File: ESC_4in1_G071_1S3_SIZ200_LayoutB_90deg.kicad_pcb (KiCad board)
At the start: 4 copper layers, 26 x 27 mm, 150 parts, among them J1 Conn_01x08, U1 STM32G071GBU6, U10 NCP81161MNTBG, U11 SIZ200DT-T1-GE3, U12 NCP81161MNTBG, U13 SIZ200DT-T1-GE3, U14 TPS630701, U15 TPS72733DSE, U16 INA185, U17 STM32G071GBU6, U18 NCP81161MNTBG, U19 SIZ200DT-T1-GE3, U2 NCP81161MNTBG, U20 NCP81161MNTBG, U21 STM32G071GBU6, U22 SIZ200DT-T1-GE3, U23 NCP81161MNTBG, U24 SIZ200DT-T1-GE3, U25 NCP81161MNTBG, U26 SIZ200DT-T1-GE3, U27 NCP81161MNTBG, U28 STM32G071GBU6, U29 SIZ200DT-T1-GE3, U3 SIZ200DT-T1-GE3, U30 NCP81161MNTBG, U31 SIZ200DT-T1-GE3, U4 NCP81161MNTBG, U5 SIZ200DT-T1-GE3, U6 NCP81161MNTBG, U7 SIZ200DT-T1-GE3, U8 NCP81161MNTBG, U9 SIZ200DT-T1-GE3

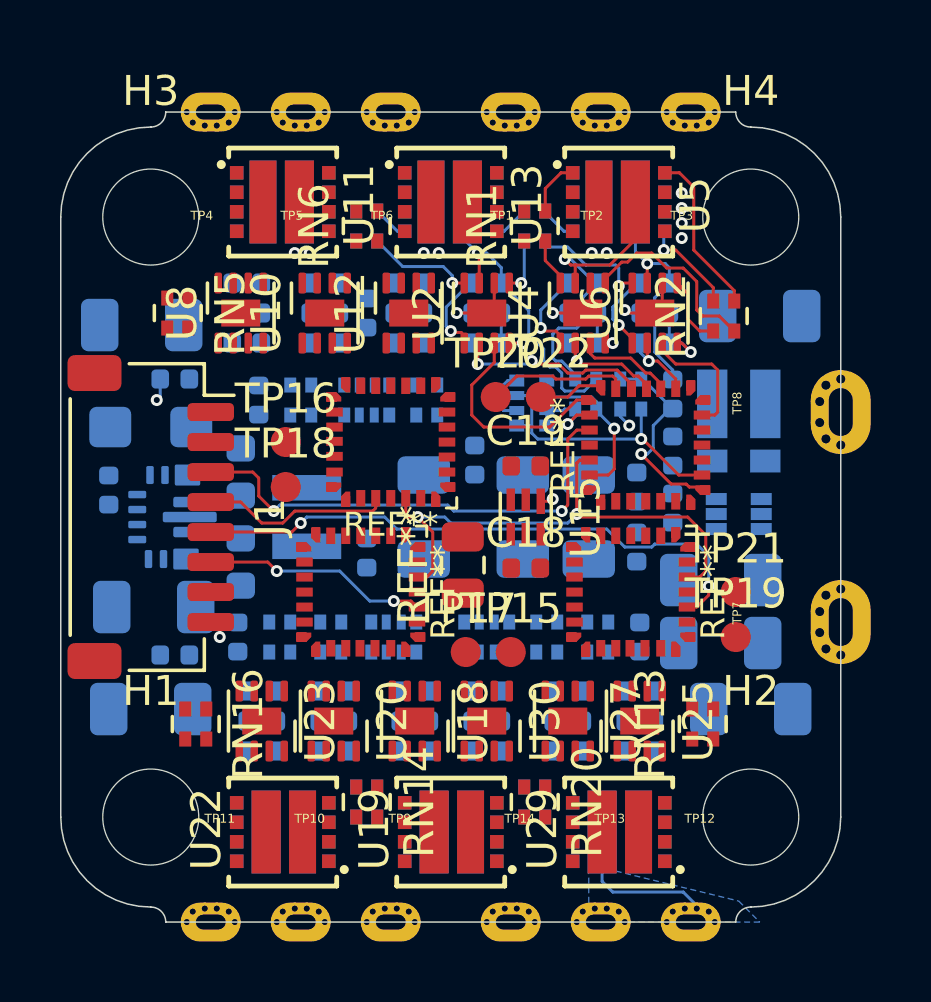
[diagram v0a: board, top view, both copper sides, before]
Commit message: - ESC1 pinout updated - ESC1 schematic done - ESC1 routed - increased PCB size to 26*27 mm
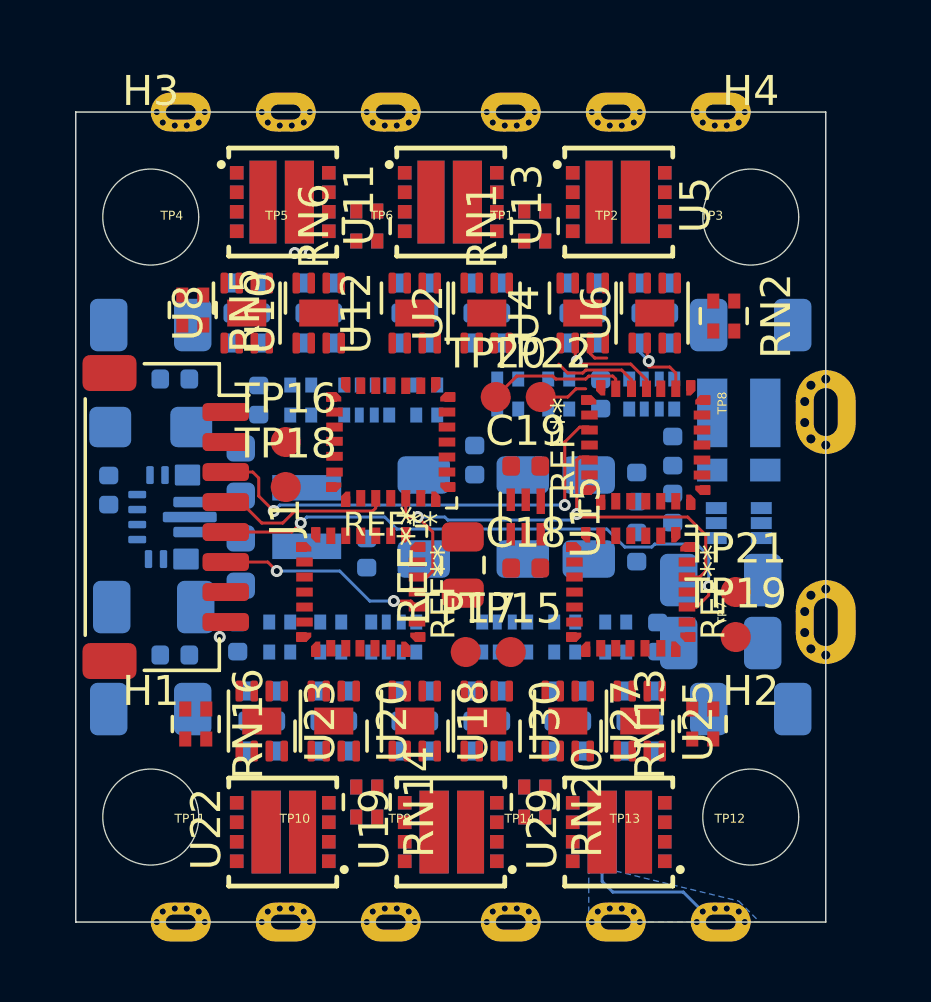
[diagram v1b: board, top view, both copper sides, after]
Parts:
- removed the REF** at (133.2, 68.2)
- moved RN9 4.01 mm to (142.7, 70.9), turned to 270 degrees
- moved RN8 2.60 mm to (137.9, 70.9)
- moved R6 2.40 mm to (141.0, 70.9)
- moved RN7 2.40 mm to (139.6, 70.9)
- moved TP11 1.00 mm to (127.0, 88.5)
- moved TP12 1.00 mm to (145.0, 88.5)
- moved TP3 1.00 mm to (145.0, 61.5)
- moved TP4 1.00 mm to (127.0, 61.5)
- moved RN23 0.60 mm to (139.8, 79.0)
- moved RN24 0.60 mm to (137.8, 79.0)
- moved R18 0.60 mm to (142.9, 79.0)
- moved RN21 0.60 mm to (141.5, 79.0)
- moved RN5 0.51 mm to (127.4, 68.1)
- moved J1 0.50 mm to (126.5, 75.0)
- moved TP10 0.50 mm to (130.5, 88.5)
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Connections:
- RN2 pad 1: /ESC1_C_DRVL -> Net-(RN2-Pad1)
- RN2 pad 2: /ESC1_B_DRVL -> Net-(RN2-Pad2)
- RN2 pad 3: /ESC1_B_GL -> Net-(RN2-Pad3)
- RN2 pad 4: /ESC1_C_GL -> Net-(RN2-Pad4)
- U1 pad 14: Net-(U1-Pad14) -> /ESC1_B_EN
- U1 pad 15: Net-(U1-Pad15) -> /ESC1_A_EN
- U1 pad 17: /ESC1_B_EN -> Net-(U1-Pad17)
- U1 pad 22: /ESC1_A_EN -> Net-(U1-Pad22)
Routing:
- net /ESC1_B: track 10.6 -> 0.00 mm, vias 1 -> 0
- net GND: track 10.4 -> 0.00 mm, vias 9 -> 1
- net /ESC1_A: track 10.2 -> 0.00 mm, vias 1 -> 0
- net /ESC1_Y: track 9.49 -> 0.00 mm, vias 1 -> 0
- net /ESC1_C: track 7.83 -> 0.00 mm, vias 1 -> 0
- net +5V: track 7.09 -> 0.00 mm, vias 4 -> 0
- net /ESC1_A_EN: track 7.07 -> 0.00 mm
- net /ESC1_MC: track 6.90 -> 0.00 mm, vias 1 -> 0
- net /ESC1_B_DRVL: track 6.44 -> 0.00 mm
- net /ESC1_MA: track 5.64 -> 0.00 mm, vias 1 -> 0
- net /ESC1_B_GL: track 5.52 -> 0.00 mm
- net /ESC1_C_EN: track 4.34 -> 0.00 mm
- net /ESC1_C_DRVH: track 4.00 -> 0.00 mm, vias 1 -> 0
- net /ESC1_A_DRVH: track 3.63 -> 0.00 mm, vias 1 -> 0
- net /ESC1_A_PWM: track 6.34 -> 2.93 mm, vias 2 -> 0
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- removed copper zone on In1.Cu_(power), net +3V3
- removed copper zone on In1.Cu_(power), net +5V
- removed copper zone on In1.Cu_(power), net +BATT
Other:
- board size 26 x 27 mm -> 25 x 27 mm
